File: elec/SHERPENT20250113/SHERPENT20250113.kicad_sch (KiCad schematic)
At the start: 129 parts, among them J1 2137160001, J2 Conn_01x03_Socket, J3 Conn_01x03_Socket, Q1 NMOS, Q2 PMOS, Q3 NMOS, Q4 PMOS, SW1 CT1102, SW2 SW_Push, U1 MCP73831T-2ACI_OT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

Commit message: Mise à jour des netclass
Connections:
- net +9V: now also C15.1, U5.3 (VI)
- net VDIODE: no longer C15.1, U5.3 (VI)
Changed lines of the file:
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@@
 	(paper "A2")
 	(junction
+		(at 251.46 321.31)
+		(diameter 0)
+		(color 0 0 0 0)
+	)
+	(junction
 		(at 425.45 298.45)
 		(diameter 0)
@@
 	)
 	(junction
-		(at 165.1 318.77)
-		(diameter 0)
-		(color 0 0 0 0)
-	)
-	(junction
 		(at 469.9 105.41)
 		(diameter 0)
@@
 	)
 	(junction
-		(at 251.46 321.31)
-		(diameter 0)
-		(color 0 0 0 0)
-	)
-	(junction
 		(at 95.25 346.71)
 		(diameter 0)
@@
 	(wire
 		(pts
-			(xy 165.1 318.77) (xy 165.1 320.04)
-		)
-		(stroke
-			(width 0)
-			(type default)
-		)
-	)
-	(wire
-		(pts
 			(xy 119.38 346.71) (xy 119.38 349.25)
 		)
@@
 	(wire
 		(pts
-			(xy 248.92 321.31) (xy 251.46 321.31)
-		)
-		(stroke
-			(width 0)
-			(type default)
-		)
-	)
-	(wire
-		(pts
 			(xy 529.59 267.97) (xy 543.56 267.97)
 		)
@@
 		)
 	)
-	(label "VDIODE"
-		(at 248.92 321.31 180)
-		(fields_autoplaced yes)
-		(effects
-			(font
-				(size 1.27 1.27)
-			)
-			(justify right bottom)
-		)
-	)
 	(label "NEOPX"
 		(at 361.95 267.97 0)
@@
 					(unit 1)
 				)
+			)
+		)
+	)
+	(symbol
+		(lib_id "power:+9V")
+		(at 251.46 321.31 0)
+		(unit 1)
+		(exclude_from_sim no)
+		(in_bom yes)
+		(on_board yes)
+		(dnp no)
+		(fields_autoplaced yes)
+		(property "Reference" "#PWR0118"
+			(at 251.46 325.12 0)
+			(effects
+				(font
+					(size 1.27 1.27)
+				)
+				(hide yes)
+			)
+		)
+		(property "Value" "+9V"
+			(at 251.46 316.23 0)
+			(effects
+				(font
+					(size 1.27 1.27)
+				)
+			)
+		)
+		(property "Footprint" ""
+			(at 251.46 321.31 0)
+			(effects
+				(font
+					(size 1.27 1.27)
+				)
+				(hide yes)
+			)
+		)
+		(property "Datasheet" ""
+			(at 251.46 321.31 0)
+			(effects
+				(font
+					(size 1.27 1.27)
+				)
+				(hide yes)
+			)
+		)
+		(property "Description" "Power symbol creates a global label with name \"+9V\""
+			(at 251.46 321.31 0)
+			(effects
+				(font
+					(size 1.27 1.27)
+				)
+				(hide yes)
+			)
+		)
+		(pin "1"
+		)
+		(instances
+			(project "SHERPENT20250113"
+				(path "/b9eec091-4b52-44a1-b170-afda02802a46"
+					(reference "#PWR0118")
+					(unit 1)
+				)

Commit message: Sauvegarde pre-tutorat
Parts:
- C12: value 91p -> 100p
- R11: value 51.1k -> 45.3k
- R12: value 523k -> 357k
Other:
- moved on the sheet: C13, R9
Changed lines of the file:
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@@
 	)
 	(junction
-		(at 119.38 336.55)
-		(diameter 0)
-		(color 0 0 0 0)
-	)
-	(junction
 		(at 69.85 274.32)
 		(diameter 0)
@@
 	)
 	(junction
+		(at 114.3 336.55)
+		(diameter 0)
+		(color 0 0 0 0)
+	)
+	(junction
 		(at 125.73 323.85)
 		(diameter 0)
@@
 	(wire
 		(pts
-			(xy 100.33 336.55) (xy 119.38 336.55)
+			(xy 100.33 336.55) (xy 114.3 336.55)
 		)
 		(stroke
@@
 	(wire
 		(pts
+			(xy 114.3 336.55) (xy 129.54 336.55)
+		)
+		(stroke
+			(width 0)
+			(type default)
+		)
+	)
+	(wire
+		(pts
 			(xy 111.76 323.85) (xy 118.11 323.85)
 		)
@@
 	(wire
 		(pts
-			(xy 119.38 346.71) (xy 119.38 349.25)
+			(xy 114.3 345.44) (xy 114.3 347.98)
 		)
 		(stroke
@@
 	(wire
 		(pts
-			(xy 119.38 336.55) (xy 119.38 339.09)
+			(xy 114.3 336.55) (xy 114.3 337.82)
 		)
 		(stroke
@@
 	(wire
 		(pts
-			(xy 119.38 336.55) (xy 129.54 336.55)
-		)
-		(stroke
-			(width 0)
-			(type default)
-		)
-	)
-	(wire
-		(pts
 			(xy 429.26 252.73) (xy 425.45 252.73)
 		)
@@
 			)
 		)
-		(property "Value" "523k"
+		(property "Value" "357k"
 			(at 193.04 321.056 0)
 			(effects
@@
 	(symbol
 		(lib_id "power:+9V")
-		(at 201.93 316.23 0)
+		(at 207.01 316.23 0)
 		(unit 1)
 		(exclude_from_sim no)
@@
 		(fields_autoplaced yes)
 		(property "Reference" "#PWR041"
-			(at 201.93 320.04 0)
+			(at 207.01 320.04 0)
 			(effects
 				(font
@@
 		)
 		(property "Value" "+9V"
-			(at 201.93 311.15 0)
+			(at 207.01 311.15 0)
 			(effects
 				(font
@@
 		)
 		(property "Footprint" ""
-			(at 201.93 316.23 0)
+			(at 207.01 316.23 0)
 			(effects
 				(font
@@
 		)
 		(property "Datasheet" ""
-			(at 201.93 316.23 0)
+			(at 207.01 316.23 0)
 			(effects
 				(font
@@
 		)
 		(property "Description" "Power symbol creates a global label with name \"+9V\""
-			(at 201.93 316.23 0)
+			(at 207.01 316.23 0)
 			(effects
 				(font
@@
 	(symbol
 		(lib_id "power:GND")
-		(at 201.93 323.85 0)
+		(at 207.01 323.85 0)
 		(unit 1)
 		(exclude_from_sim no)
@@
 		(dnp no)
 		(property "Reference" "#PWR042"
-			(at 201.93 330.2 0)
+			(at 207.01 330.2 0)
 			(effects
 				(font
@@
 		)
 		(property "Value" "GND"
-			(at 204.978 327.152 0)
+			(at 210.058 327.152 0)
 			(effects
 				(font
@@
 		)
 		(property "Footprint" ""
-			(at 201.93 323.85 0)
+			(at 207.01 323.85 0)
 			(effects
 				(font
@@
 		)
 		(property "Datasheet" ""
-			(at 201.93 323.85 0)
+			(at 207.01 323.85 0)
 			(effects
 				(font
@@
 		)
 		(property "Description" "Power symbol creates a global label with name \"GND\" , ground"
-			(at 201.93 323.85 0)
+			(at 207.01 323.85 0)
 			(effects
 				(font
@@
 	(symbol
 		(lib_id "power:GND")
-		(at 119.38 349.25 0)
+		(at 114.3 347.98 0)
 		(unit 1)
 		(exclude_from_sim no)
@@
 		(dnp no)
 		(property "Reference" "#PWR016"
-			(at 119.38 355.6 0)
+			(at 114.3 354.33 0)
 			(effects
 				(font
@@
 		)
 		(property "Value" "GND"
-			(at 119.38 353.06 0)
+			(at 114.3 351.79 0)
 			(effects
 				(font
@@
 		)
 		(property "Footprint" ""
-			(at 119.38 349.25 0)
+			(at 114.3 347.98 0)
 			(effects
 				(font
@@
 		)
 		(property "Datasheet" ""
-			(at 119.38 349.25 0)
+			(at 114.3 347.98 0)
 			(effects
 				(font
@@
 		)
 		(property "Description" "Power symbol creates a global label with name \"GND\" , ground"
-			(at 119.38 349.25 0)
+			(at 114.3 347.98 0)
 			(effects
 				(font
@@
 			)
 		)
-		(property "Value" "91p"
+		(property "Value" "100p"
 			(at 187.706 339.09 0)
 			(effects
@@
 			)
 		)
-		(property "Value" "51.1k"
+		(property "Value" "45.3k"
 			(at 177.8 333.756 0)
 			(effects
@@
 	(symbol
 		(lib_id "Device:R_US")
-		(at 119.38 342.9 0)
+		(at 114.3 341.63 0)
 		(unit 1)
 		(exclude_from_sim no)
@@
 		(dnp no)
 		(property "Reference" "R9"
-			(at 120.65 341.884 0)
+			(at 115.57 340.614 0)
 			(effects
 				(font
@@
 		)
 		(property "Value" "10k"
-			(at 120.65 343.916 0)
+			(at 115.57 342.646 0)
 			(effects
 				(font
@@
 		)
 		(property "Footprint" "Resistor_SMD:R_0603_1608Metric"
-			(at 120.396 343.154 90)
+			(at 115.316 341.884 90)
 			(effects
 				(font
@@
 		)
 		(property "Datasheet" "~"
-			(at 119.38 342.9 0)
+			(at 114.3 341.63 0)
 			(effects
 				(font
@@
 		)
 		(property "Description" "Resistor, US symbol"
-			(at 119.38 342.9 0)
+			(at 114.3 341.63 0)
 			(effects
 				(font
@@
 	(symbol
 		(lib_id "Device:C")
-		(at 201.93 320.04 0)
+		(at 207.01 320.04 0)
 		(unit 1)
 		(exclude_from_sim no)
@@
 		(dnp no)
 		(property "Reference" "C13"
-			(at 195.58 318.77 0)
+			(at 200.66 318.77 0)
 			(effects
 				(font
@@
 		)
 		(property "Value" "47u"
-			(at 195.58 321.31 0)
+			(at 200.66 321.31 0)
 			(effects
 				(font
@@
 		)
 		(property "Footprint" "Capacitor_SMD:C_0603_1608Metric_Pad1.08x0.95mm_HandSolder"
-			(at 202.8952 323.85 0)
+			(at 207.9752 323.85 0)
 			(effects
 				(font
@@
 		)
 		(property "Datasheet" "~"
-			(at 201.93 320.04 0)
+			(at 207.01 320.04 0)
 			(effects
 				(font
@@
 		)
 		(property "Description" "Unpolarized capacitor"
-			(at 201.93 320.04 0)
+			(at 207.01 320.04 0)
 			(effects
 				(font

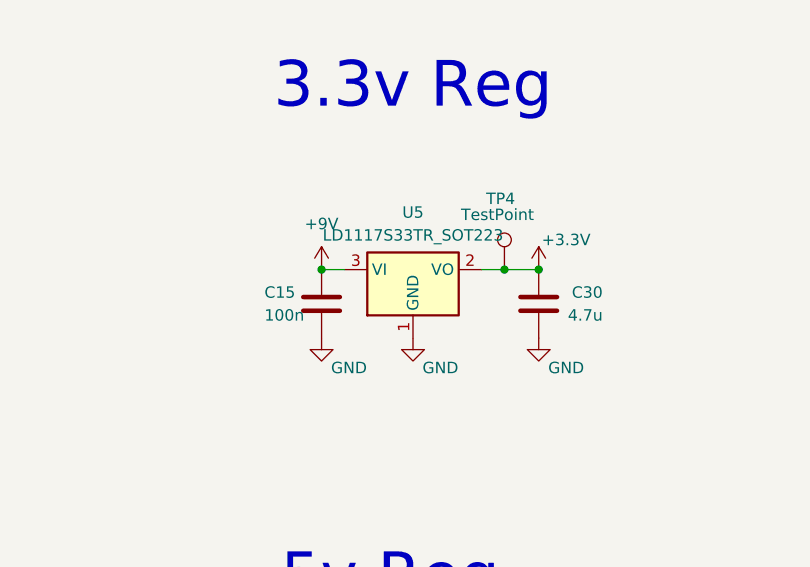
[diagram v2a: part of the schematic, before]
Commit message: Ajout du thermal relief sur le buck dcdc converter
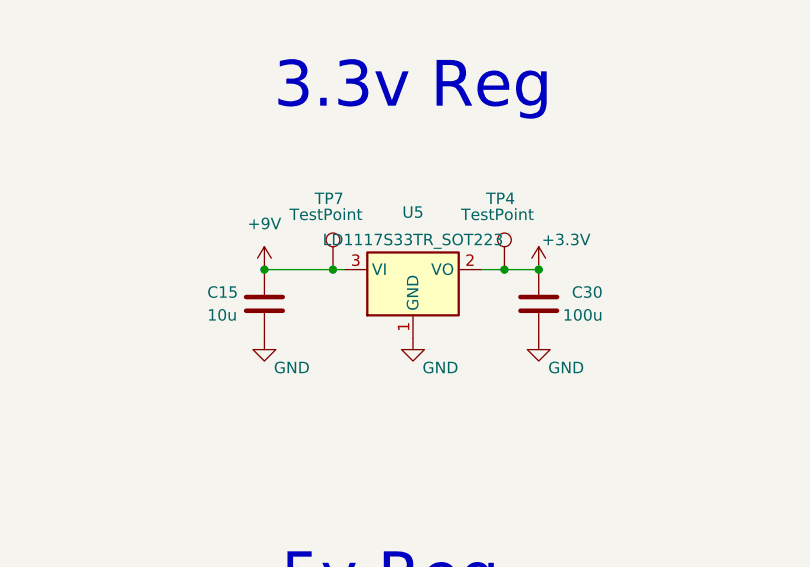
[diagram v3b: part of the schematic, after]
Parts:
- added TP7: TestPoint, TestPoint:TestPoint_Loop_D2.54mm_Drill1.5mm_Beaded, symbol Connector:TestPoint
- C15: value 100n -> 10u
- C30: value 4.7u -> 100u
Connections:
- net +9V: now also TP7.1
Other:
- moved on the sheet: C15
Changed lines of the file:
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@@
 	(paper "A2")
 	(junction
-		(at 251.46 321.31)
+		(at 245.11 321.31)
 		(diameter 0)
 		(color 0 0 0 0)
@@
 	)
 	(junction
+		(at 252.73 321.31)
+		(diameter 0)
+		(color 0 0 0 0)
+	)
+	(junction
 		(at 514.35 298.45)
 		(diameter 0)
@@
 	(wire
 		(pts
+			(xy 252.73 321.31) (xy 254 321.31)
+		)
+		(stroke
+			(width 0)
+			(type default)
+		)
+	)
+	(wire
+		(pts
 			(xy 461.01 252.73) (xy 461.01 267.97)
 		)
@@
 	(wire
 		(pts
-			(xy 251.46 321.31) (xy 254 321.31)
+			(xy 245.11 321.31) (xy 252.73 321.31)
 		)
 		(stroke
@@
 	(symbol
 		(lib_id "power:GND")
-		(at 251.46 328.93 0)
+		(at 245.11 328.93 0)
 		(unit 1)
 		(exclude_from_sim no)
@@
 		(dnp no)
 		(property "Reference" "#PWR0109"
-			(at 251.46 335.28 0)
+			(at 245.11 335.28 0)
 			(effects
 				(font
@@
 		)
 		(property "Value" "GND"
-			(at 254.508 332.232 0)
+			(at 248.158 332.232 0)
 			(effects
 				(font
@@
 		)
 		(property "Footprint" ""
-			(at 251.46 328.93 0)
+			(at 245.11 328.93 0)
 			(effects
 				(font
@@
 		)
 		(property "Datasheet" ""
-			(at 251.46 328.93 0)
+			(at 245.11 328.93 0)
 			(effects
 				(font
@@
 		)
 		(property "Description" "Power symbol creates a global label with name \"GND\" , ground"
-			(at 251.46 328.93 0)
+			(at 245.11 328.93 0)
 			(effects
 				(font
@@
 			)
 		)
-		(property "Value" "4.7u"
+		(property "Value" "100u"
 			(at 282.702 326.39 0)
 			(effects
@@
 		(on_board yes)
 		(dnp no)
-		(fields_autoplaced yes)
 		(property "Reference" "U5"
 			(at 261.62 314.96 0)
@@
 		)
 		(property "Value" "LD1117S33TR_SOT223"
-			(at 261.62 317.5 0)
+			(at 261.62 318.008 0)
 			(effects
 				(font
@@
 	(symbol
 		(lib_id "Device:C")
-		(at 251.46 325.12 0)
+		(at 245.11 325.12 0)
 		(unit 1)
 		(exclude_from_sim no)
@@
 		(dnp no)
 		(property "Reference" "C15"
-			(at 245.11 323.85 0)
+			(at 238.76 323.85 0)
 			(effects
 				(font
@@
 			)
 		)
-		(property "Value" "100n"
-			(at 245.11 326.39 0)
+		(property "Value" "10u"
+			(at 238.76 326.39 0)
 			(effects
 				(font
@@
 		)
 		(property "Footprint" "Capacitor_SMD:C_0603_1608Metric_Pad1.08x0.95mm_HandSolder"
-			(at 252.4252 328.93 0)
+			(at 246.0752 328.93 0)
 			(effects
 				(font
@@
 		)
 		(property "Datasheet" "~"
-			(at 251.46 325.12 0)
+			(at 245.11 325.12 0)
 			(effects
 				(font
@@
 		)
 		(property "Description" "Unpolarized capacitor"
-			(at 251.46 325.12 0)
+			(at 245.11 325.12 0)
 			(effects
 				(font
@@
 	(symbol
 		(lib_id "power:+9V")
-		(at 251.46 321.31 0)
+		(at 245.11 321.31 0)
 		(unit 1)
 		(exclude_from_sim no)
@@
 		(fields_autoplaced yes)
 		(property "Reference" "#PWR0118"
-			(at 251.46 325.12 0)
+			(at 245.11 325.12 0)
 			(effects
 				(font
@@
 		)
 		(property "Value" "+9V"
-			(at 251.46 316.23 0)
+			(at 245.11 316.23 0)
 			(effects
 				(font
@@
 		)
 		(property "Footprint" ""
-			(at 251.46 321.31 0)
+			(at 245.11 321.31 0)
 			(effects
 				(font
@@
 		)
 		(property "Datasheet" ""
-			(at 251.46 321.31 0)
+			(at 245.11 321.31 0)
 			(effects
 				(font
@@
 		)
 		(property "Description" "Power symbol creates a global label with name \"+9V\""
-			(at 251.46 321.31 0)
+			(at 245.11 321.31 0)
 			(effects
 				(font
@@
 					(unit 1)
 				)
+			)
+		)
+	)
+	(symbol
+		(lib_id "Connector:TestPoint")
+		(at 252.73 321.31 0)
+		(unit 1)
+		(exclude_from_sim no)
+		(in_bom yes)
+		(on_board yes)
+		(dnp no)
+		(property "Reference" "TP7"
+			(at 250.698 313.436 0)
+			(effects
+				(font
+					(size 1.27 1.27)
+				)
+				(justify left)
+			)
+		)
+		(property "Value" "TestPoint"
+			(at 247.904 315.214 0)
+			(effects
+				(font
+					(size 1.27 1.27)
+				)
+				(justify left)
+			)
+		)
+		(property "Footprint" "TestPoint:TestPoint_Loop_D2.54mm_Drill1.5mm_Beaded"
+			(at 257.81 321.31 0)
+			(effects
+				(font
+					(size 1.27 1.27)
+				)
+				(hide yes)
+			)
+		)
+		(property "Datasheet" "~"
+			(at 257.81 321.31 0)
+			(effects
+				(font
+					(size 1.27 1.27)
+				)
+				(hide yes)
+			)
+		)
+		(property "Description" ""
+			(at 252.73 321.31 0)
+			(effects
+				(font
+					(size 1.27 1.27)
+				)
+				(hide yes)
+			)
+		)
+		(pin "1"
+		)
+		(instances
+			(project "SHERPENT20250113"
+				(path "/b9eec091-4b52-44a1-b170-afda02802a46"
+					(reference "TP7")
+					(unit 1)
+				)

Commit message: Modification simple sur la layout, buck-boost
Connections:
- net I2C_DO is gone; now on net VBATT: U7.27 (U0RXD)
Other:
- moved on the sheet: BT1, BT2, F1
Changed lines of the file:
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@@
 	)
 	(junction
-		(at 76.2 323.85)
-		(diameter 0)
-		(color 0 0 0 0)
-	)
-	(junction
 		(at 275.59 321.31)
 		(diameter 0)
@@
 	)
 	(junction
-		(at 157.48 76.2)
+		(at 157.48 69.85)
 		(diameter 0)
 		(color 0 0 0 0)
@@
 	)
 	(junction
+		(at 76.2 323.85)
+		(diameter 0)
+		(color 0 0 0 0)
+	)
+	(junction
 		(at 372.11 298.45)
 		(diameter 0)
@@
 	(wire
 		(pts
-			(xy 167.64 76.2) (xy 170.18 76.2)
+			(xy 167.64 69.85) (xy 173.99 69.85)
 		)
 		(stroke
@@
 	(wire
 		(pts
-			(xy 157.48 76.2) (xy 160.02 76.2)
+			(xy 157.48 69.85) (xy 160.02 69.85)
 		)
 		(stroke
@@
 	(wire
 		(pts
-			(xy 157.48 76.2) (xy 157.48 80.01)
+			(xy 157.48 69.85) (xy 157.48 73.66)
 		)
 		(stroke
@@
 	(wire
 		(pts
-			(xy 151.13 76.2) (xy 151.13 80.01)
+			(xy 151.13 69.85) (xy 151.13 73.66)
 		)
 		(stroke
@@
 	(wire
 		(pts
-			(xy 157.48 87.63) (xy 157.48 88.9)
+			(xy 157.48 81.28) (xy 157.48 82.55)
 		)
 		(stroke
@@
 	(wire
 		(pts
-			(xy 151.13 76.2) (xy 157.48 76.2)
+			(xy 151.13 69.85) (xy 157.48 69.85)
 		)
 		(stroke
@@
 	(wire
 		(pts
-			(xy 151.13 88.9) (xy 151.13 87.63)
+			(xy 151.13 82.55) (xy 151.13 81.28)
 		)
 		(stroke
@@
 	(wire
 		(pts
-			(xy 59.69 323.85) (xy 76.2 323.85)
+			(xy 40.64 323.85) (xy 76.2 323.85)
 		)
 		(stroke
@@
 	(text "Battery"
 		(exclude_from_sim no)
-		(at 161.29 64.77 0)
+		(at 161.29 58.42 0)
 		(effects
 			(font
@@
 		)
 	)
-	(label "I2C_DO"
-		(at 434.34 100.33 180)
+	(label "VBATT"
+		(at 173.99 69.85 180)
 		(fields_autoplaced yes)
 		(effects
@@
 	)
 	(label "VBATT"
-		(at 59.69 323.85 0)
+		(at 40.64 323.85 0)
 		(fields_autoplaced yes)
 		(effects
@@
 		)
 	)
-	(global_label "VBATT"
-		(shape input)
-		(at 170.18 76.2 0)
+	(label "VBATT"
+		(at 434.34 100.33 180)
 		(fields_autoplaced yes)
 		(effects
@@
 				(size 1.27 1.27)
 			)
-			(justify left)
-		)
-		(property "Intersheetrefs" "${INTERSHEET_REFS}"
-			(at 178.5476 76.2 0)
-			(effects
-				(font
-					(size 1.27 1.27)
-				)
-				(justify left)
-				(hide yes)
-			)
+			(justify right bottom)
 		)
 	)
@@
 	(symbol
 		(lib_id "Device:Fuse")
-		(at 163.83 76.2 90)
+		(at 163.83 69.85 90)
 		(unit 1)
 		(exclude_from_sim no)
@@
 		(fields_autoplaced yes)
 		(property "Reference" "F1"
-			(at 163.83 69.85 90)
+			(at 163.83 63.5 90)
 			(effects
 				(font
@@
 		)
 		(property "Value" "10A"
-			(at 163.83 72.39 90)
+			(at 163.83 66.04 90)
 			(effects
 				(font
@@
 		)
 		(property "Footprint" "Fuse:Fuse_0603_1608Metric"
-			(at 163.83 77.978 90)
+			(at 163.83 71.628 90)
 			(effects
 				(font
@@
 		)
 		(property "Datasheet" "~"
-			(at 163.83 76.2 0)
+			(at 163.83 69.85 0)
 			(effects
 				(font
@@
 		)
 		(property "Description" "Fuse"
-			(at 163.83 76.2 0)
+			(at 163.83 69.85 0)
 			(effects
 				(font
@@
 	(symbol
 		(lib_id "Device:Battery_Cell")
-		(at 157.48 85.09 0)
+		(at 157.48 78.74 0)
 		(unit 1)
 		(exclude_from_sim no)
@@
 		(dnp no)
 		(property "Reference" "BT2"
-			(at 162.56 81.28 0)
+			(at 162.56 74.93 0)
 			(effects
 				(font
@@
 		)
 		(property "Value" "Battery_Cell"
-			(at 152.4 83.2485 90)
+			(at 152.4 76.8985 90)
 			(effects
 				(font
@@
 		)
 		(property "Footprint" "Connector_PinHeader_2.54mm:PinHeader_1x02_P2.54mm_Vertical"
-			(at 157.48 83.566 90)
+			(at 157.48 77.216 90)
 			(effects
 				(font
@@
 		)
 		(property "Datasheet" "~"
-			(at 157.48 83.566 90)
+			(at 157.48 77.216 90)
 			(effects
 				(font
@@
 		)
 		(property "Description" "Single-cell battery"
-			(at 157.48 85.09 0)
+			(at 157.48 78.74 0)
 			(effects
 				(font
@@
 	(symbol
 		(lib_id "power:GND")
-		(at 151.13 88.9 0)
+		(at 151.13 82.55 0)
 		(unit 1)
 		(exclude_from_sim no)
@@
 		(dnp no)
 		(property "Reference" "#PWR024"
-			(at 151.13 95.25 0)
+			(at 151.13 88.9 0)
 			(effects
 				(font
@@
 		)
 		(property "Value" "GND"
-			(at 151.13 92.71 0)
+			(at 151.13 86.36 0)
 			(effects
 				(font
@@
 		)
 		(property "Footprint" ""
-			(at 151.13 88.9 0)
+			(at 151.13 82.55 0)
 			(effects
 				(font
@@
 		)
 		(property "Datasheet" ""
-			(at 151.13 88.9 0)
+			(at 151.13 82.55 0)
 			(effects
 				(font
@@
 		)
 		(property "Description" "Power symbol creates a global label with name \"GND\" , ground"
-			(at 151.13 88.9 0)
+			(at 151.13 82.55 0)
 			(effects
 				(font
@@
 	(symbol
 		(lib_id "power:GND")
-		(at 157.48 88.9 0)
+		(at 157.48 82.55 0)
 		(unit 1)
 		(exclude_from_sim no)
@@
 		(dnp no)
 		(property "Reference" "#PWR029"
-			(at 157.48 95.25 0)
+			(at 157.48 88.9 0)
 			(effects
 				(font
@@
 		)
 		(property "Value" "GND"
-			(at 157.48 92.71 0)
+			(at 157.48 86.36 0)
 			(effects
 				(font
@@
 		)
 		(property "Footprint" ""
-			(at 157.48 88.9 0)
+			(at 157.48 82.55 0)
 			(effects
 				(font
@@
 		)
 		(property "Datasheet" ""
-			(at 157.48 88.9 0)
+			(at 157.48 82.55 0)
 			(effects
 				(font
@@
 		)
 		(property "Description" "Power symbol creates a global label with name \"GND\" , ground"
-			(at 157.48 88.9 0)
+			(at 157.48 82.55 0)
 			(effects
 				(font
@@
 	(symbol
 		(lib_id "Device:Battery_Cell")
-		(at 151.13 85.09 0)
+		(at 151.13 78.74 0)
 		(unit 1)
 		(exclude_from_sim no)
@@
 		(dnp no)
 		(property "Reference" "BT1"
-			(at 148.59 81.28 0)
+			(at 148.59 74.93 0)
 			(effects
 				(font
@@
 		)
 		(property "Value" "Battery_Cell"
-			(at 162.56 83.82 90)
+			(at 162.56 77.47 90)
 			(effects
 				(font
@@
 		)
 		(property "Footprint" "Connector_PinHeader_2.54mm:PinHeader_1x02_P2.54mm_Vertical"
-			(at 151.13 83.566 90)
+			(at 151.13 77.216 90)
 			(effects
 				(font
@@
 		)
 		(property "Datasheet" "~"
-			(at 151.13 83.566 90)
+			(at 151.13 77.216 90)
 			(effects
 				(font
@@
 		)
 		(property "Description" "Single-cell battery"
-			(at 151.13 85.09 0)
+			(at 151.13 78.74 0)
 			(effects
 				(font

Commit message: Ajout de la lecture de tension des cellules, grosseur des track, intégrité des signaux
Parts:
- added JP19: Jumper_2_Bridged, TestPoint:TestPoint_2Pads_Pitch2.54mm_Drill0.8mm, symbol Jumper:Jumper_2_Bridged
- added R26: 0, Resistor_SMD:R_0603_1608Metric, symbol Device:R_US
- added R27: 27.3k 0.1%, Resistor_SMD:R_0603_1608Metric, symbol Device:R_US
- added R28: 100k 0.1%, Resistor_SMD:R_0603_1608Metric, symbol Device:R_US
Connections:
- net Button: now also U7.8 (GPIO3)
- net DIODE_STATE: no longer U7.8 (GPIO3)
- net GND: now also R28.1
- net VBATT: now also JP19.2 (B), R26.1, R27.2; no longer U7.27 (U0RXD)
- net VUSB: now also JP19.1 (A)
- net at Q4.1 (D), R9.1, U2.6 (EN): now also R26.2
- new net: R27.1, R28.2, U7.27 (U0RXD)
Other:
- note added: "Ajouter une fuse entre les deux cellules?"
- note removed: "!! Placer Button sur un GPIO !!"
